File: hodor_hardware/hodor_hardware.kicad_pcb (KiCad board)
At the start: 2 copper layers, 259 parts, among them J1 Screw_Terminal_01x02, J10 Screw_Terminal_01x03, J2 Screw_Terminal_01x05, J3 Screw_Terminal_01x03, J4 USB_C_Receptacle_USB2.0_16P, J5 Screw_Terminal_01x03, J6 Screw_Terminal_01x04, J7 Screw_Terminal_01x02, J8 Conn_01x04_Pin, J9 Conn_01x04_Pin, K1 FINDER-32.21-x000, K2 FINDER-32.21-x000, Q1 SiS443DN, Q10 BC847BDW1, Q2 FDG1024NZ, Q3 FDG1024NZ, Q4 FDG1024NZ, Q5 BSS138, Q6 BSS138DW, Q7 SiS443DN, Q8 2V7002, Q9 DMP6050SSD, SW1 SW_RST, SW2 SW_BOOT, T1 GND, T10 V_{BUS}, T11 3V3, T12 5V, T14 V_{BUS}_SENSE, T15 I_SNS, T16 D_FB, T17 D_PWM2, T18 D_PWM1, T19 VC_OUT, T20 V_LDSNS, T21 SCL, T22 VC_CMP, T23 VC_REF, T24 SDA, T25 DRV_EN, T26 DRV_SF, T27 SF_Q, T28 SF_TRG, T29 SF_CLR, T30 ENC_B, T31 ENC_A, T32 GND, T4 IN2, T5 IN1, T6 V_{DC}_SENSE, T7 IN3, T8 IN4, T9 V_{DC}, U1 ESP32-S3-WROOM-1_N8R2, U10 LM4040DBZ-2.5, U11 MCP6561x-LT, U12 MC33HB2002, U13 74LVC1G123, U14 ACS722xLCTR-10AB, U2 TLV62569DBV, U3 74LVC2G14, U4 74LVC2G14, U5 TPS54240DRC, U6 MAX811SEUS-T, U7 74LVC2G14, U8 ZXTR2105F, U9 24LC256

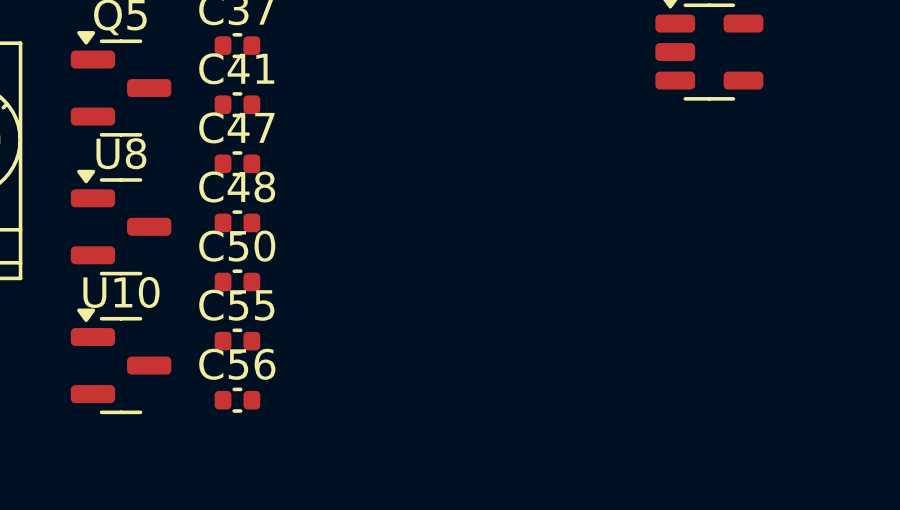
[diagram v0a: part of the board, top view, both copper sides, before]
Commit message: Added USB switchover function for 5V
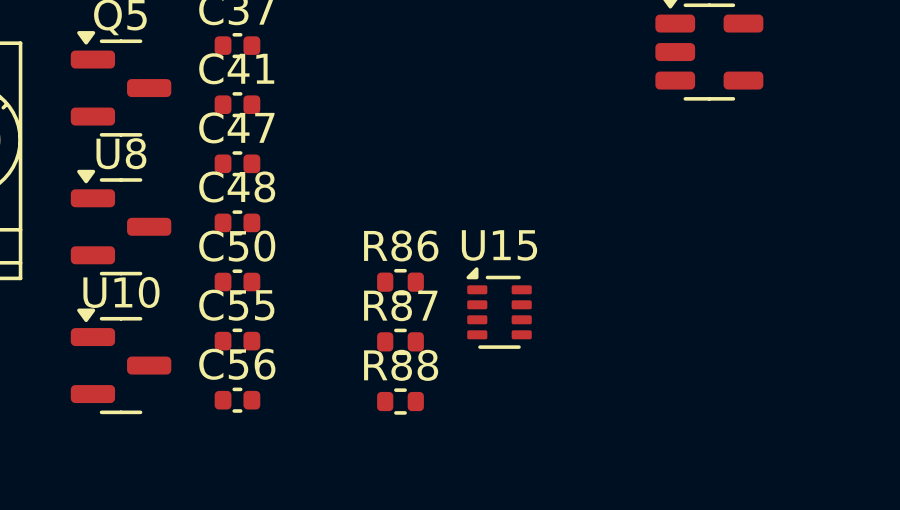
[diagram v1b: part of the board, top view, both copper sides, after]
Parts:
- added R86: 10k, Resistor_SMD:R_0402_1005Metric, F.Cu at (65.6, 114.0)
- added R87: 0R, Resistor_SMD:R_0402_1005Metric, F.Cu at (65.6, 116.0)
- added R88: 10k, Resistor_SMD:R_0402_1005Metric, F.Cu at (65.6, 118.0)
- added U15: TPS2116DRL, Package_TO_SOT_SMD:SOT-583-8, F.Cu at (68.9, 115.0)
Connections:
- C18 pad 1: Net-(D17-A) -> 5V_USB
- C19 pad 2: Net-(D17-A) -> 5V_USB
- C58 pad 1: +5V -> Net-(U15-MODE)
- C66 pad 1: +5V -> Net-(U15-MODE)
- C67 pad 1: +5V -> Net-(U15-MODE)
- C68 pad 1: +5V -> Net-(U15-MODE)
- C69 pad 1: +5V -> Net-(U15-MODE)
- C70 pad 1: +5V -> Net-(U15-MODE)
- L13 pad 2: +5V -> Net-(U15-MODE)
- L2 pad 1: Net-(D17-A) -> 5V_USB
- R73 pad 2: +5V -> Net-(U15-MODE)

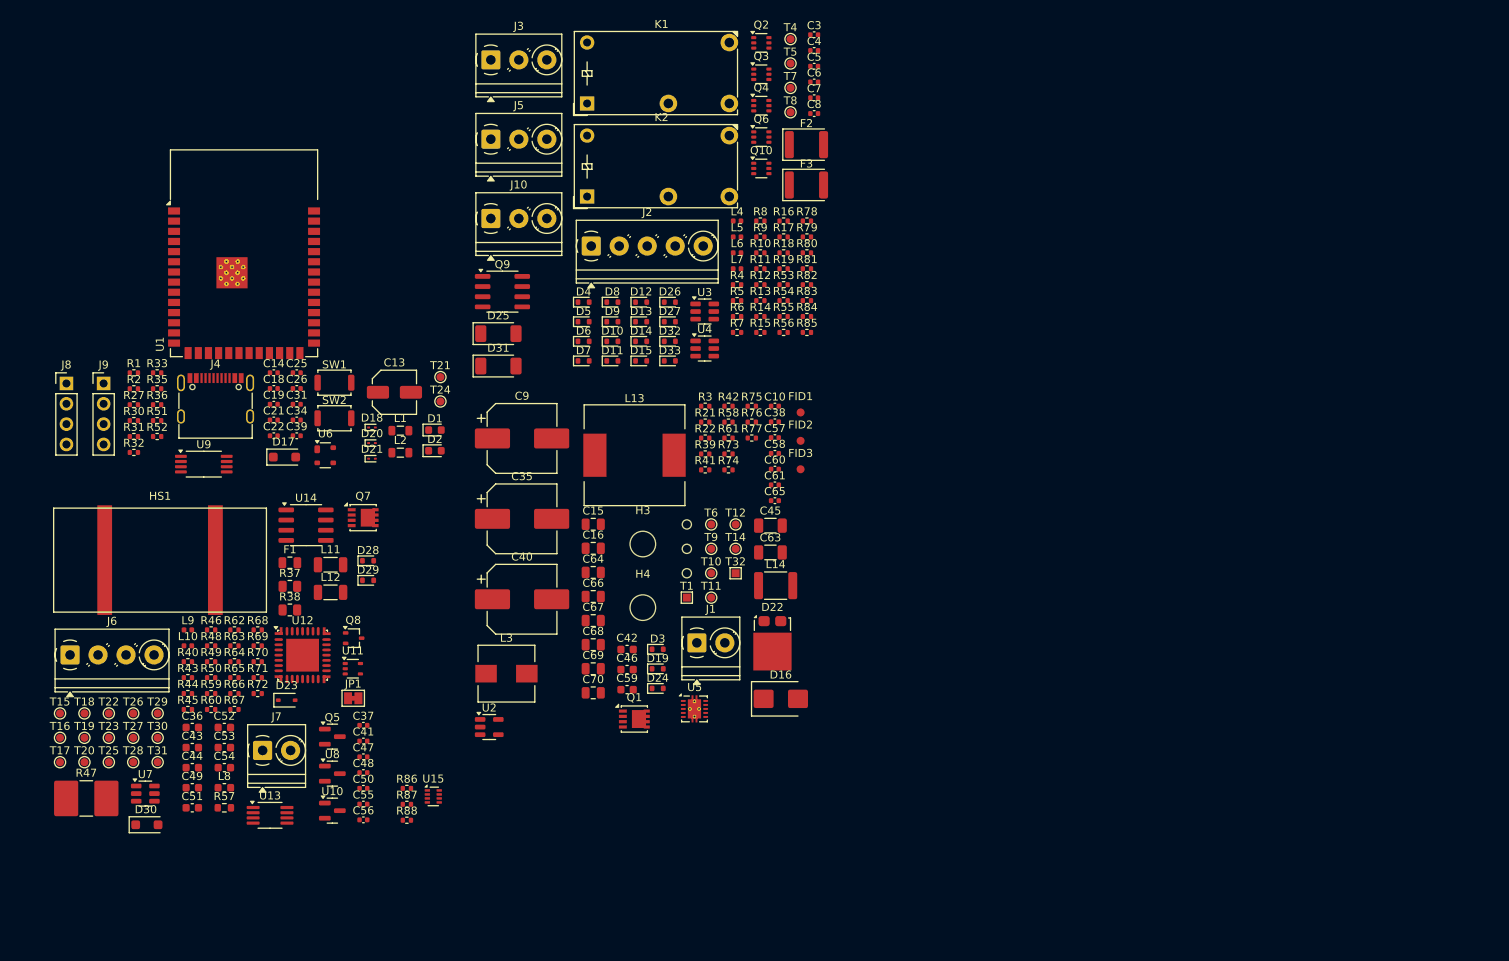
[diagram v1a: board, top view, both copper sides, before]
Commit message: Reworked into 2 PCBs
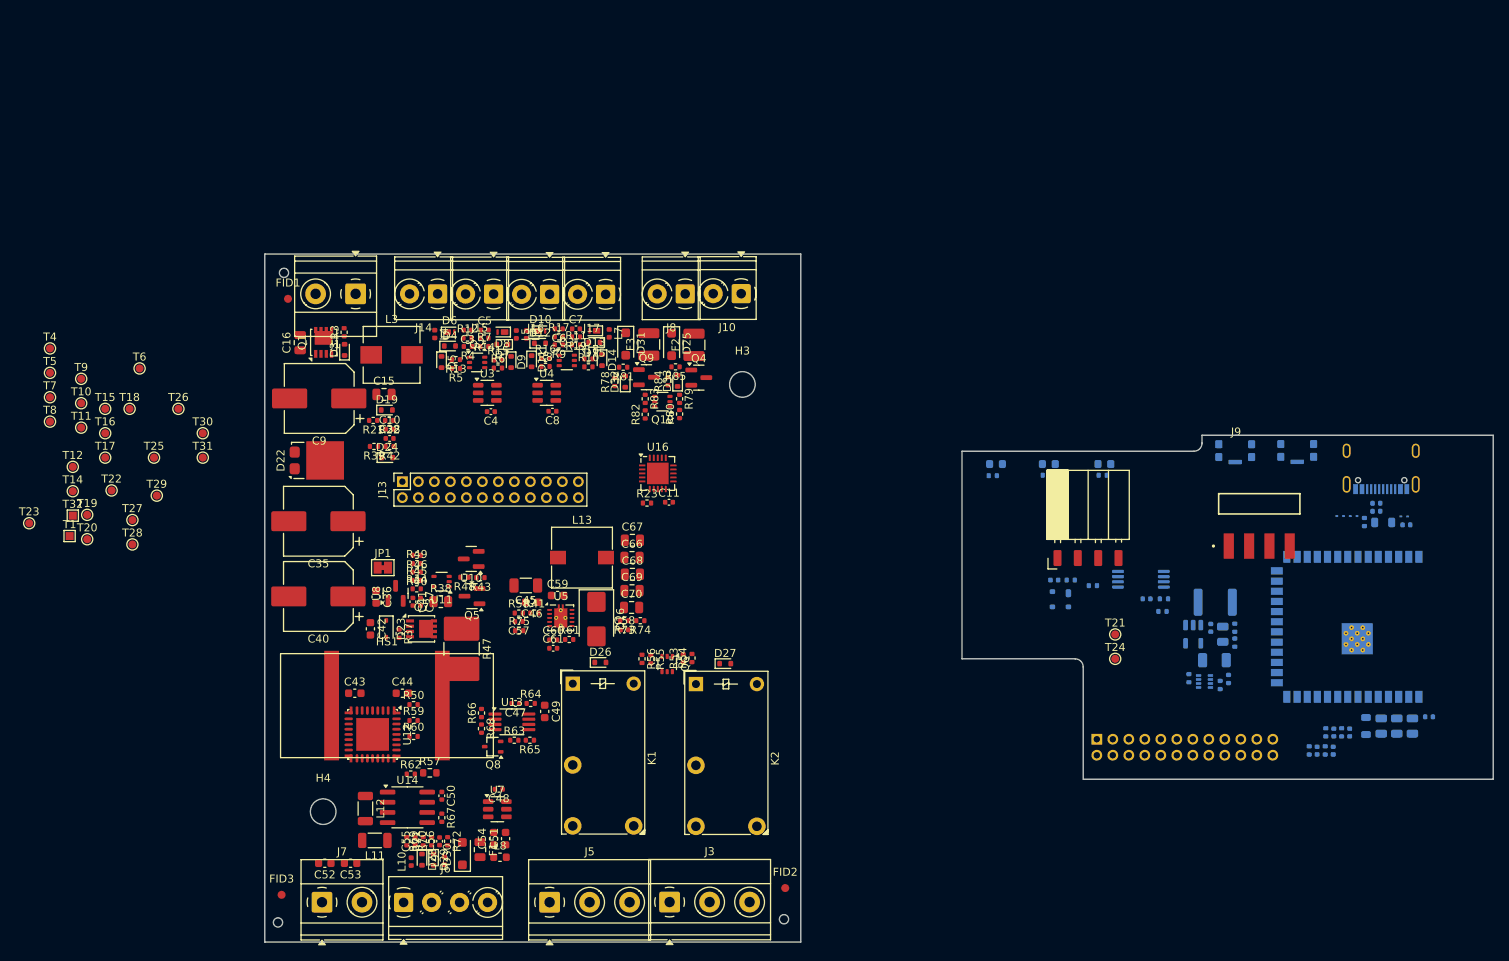
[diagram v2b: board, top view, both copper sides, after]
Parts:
- removed C13: 47u/10V, Capacitor_SMD:C_Elec_5x5.4
- removed J2: Screw_Terminal_01x05, TerminalBlock_Phoenix:TerminalBlock_Phoenix_PT-1,5-5-3.5-H_1x05_P3.50mm_Horizontal
- added C11: 100nF, Capacitor_SMD:C_0402_1005Metric, F.Cu at (98.3, 78.2)
- added C71: 10uF, Capacitor_SMD:C_0805_2012Metric, B.Cu at (187.3, 106.2)
- added C72: 10uF, Capacitor_SMD:C_0805_2012Metric, B.Cu at (189.3, 106.2)
- added C73: 10uF, Capacitor_SMD:C_0805_2012Metric, B.Cu at (191.2, 106.2)
- added J12: Conn_01x24_Pin, Connector_PinHeader_2.00mm:PinHeader_2x12_P2.00mm_Horizontal, B.Cu at (151.8, 107.8)
- added J13: Conn_01x24_Socket, Connector_PinSocket_2.00mm:PinSocket_2x12_P2.00mm_Vertical, F.Cu at (65.0, 75.7)
- added J14: Screw_Terminal_01x02, TerminalBlock_Phoenix:TerminalBlock_Phoenix_PT-1,5-2-3.5-H_1x02_P3.50mm_Horizontal, F.Cu at (69.4, 52.2)
- added J15: Screw_Terminal_01x02, TerminalBlock_Phoenix:TerminalBlock_Phoenix_PT-1,5-2-3.5-H_1x02_P3.50mm_Horizontal, F.Cu at (76.4, 52.2)
- added J16: Screw_Terminal_01x02, TerminalBlock_Phoenix:TerminalBlock_Phoenix_PT-1,5-2-3.5-H_1x02_P3.50mm_Horizontal, F.Cu at (83.4, 52.2)
- added J17: Screw_Terminal_01x02, TerminalBlock_Phoenix:TerminalBlock_Phoenix_PT-1,5-2-3.5-H_1x02_P3.50mm_Horizontal, F.Cu at (90.4, 52.2)
- added R20: 220R, Resistor_SMD:R_0402_1005Metric, B.Cu at (152.5, 74.8)
- added R23: 10k, Resistor_SMD:R_0402_1005Metric, F.Cu at (95.6, 78.3)
- added U16: MCP23S08-xML, Package_DFN_QFN:QFN-20-1EP_4x4mm_P0.5mm_EP2.7x2.7mm, F.Cu at (96.9, 74.6)
- added U17: SSD1306, hodor_footprints:SSD1306_OLED_Horizontal_Reverse, F.Cu at (150.7, 85.2)
- C14, C18, C19, C21, C22, C25, C26, C31, C34, C39, C63, C64, C65, D18, D20, D21, J4, L1, L14, L2, R1, R2, R27, R30, R31, R32, R33, R35, R36, R51, R52, R76, R77, R86, R87, R88, U1, U15, U2, U6, U9: moved to B.Cu
- D1, D2: footprint LED_SMD:LED_0603_1608Metric -> LED_SMD:LED_Kingbright_APA1606_1.6x0.6mm_Horizontal; moved to B.Cu
- D10, D13, D6, D8: footprint Diode_SMD:D_SOD-523 -> Diode_SMD:Nexperia_DSN1608-2_1.6x0.8mm
- D17: value PMEG6010 -> blue; footprint Diode_SMD:D_SOD-123F -> LED_SMD:LED_Kingbright_APA1606_1.6x0.6mm_Horizontal; moved to B.Cu
- D25, D31: footprint Diode_SMD:D_SOD-128 -> Diode_SMD:D_SOD-123F
- F2, F3: footprint Diode_SMD:D_1812_4532Metric -> Fuse:Fuse_1210_3225Metric
- J1, J7: footprint TerminalBlock_Phoenix:TerminalBlock_Phoenix_PT-1,5-2-3.5-H_1x02_P3.50mm_Horizontal -> TerminalBlock_Phoenix:TerminalBlock_Phoenix_MKDS-1,5-2_1x02_P5.00mm_Horizontal
- J10: value Screw_Terminal_01x03 -> Screw_Terminal_01x02; footprint TerminalBlock_Phoenix:TerminalBlock_Phoenix_PT-1,5-3-3.5-H_1x03_P3.50mm_Horizontal -> TerminalBlock_Phoenix:TerminalBlock_Phoenix_PT-1,5-2-3.5-H_1x02_P3.50mm_Horizontal
- J3, J5: footprint TerminalBlock_Phoenix:TerminalBlock_Phoenix_PT-1,5-3-3.5-H_1x03_P3.50mm_Horizontal -> TerminalBlock_Phoenix:TerminalBlock_Phoenix_MKDS-1,5-3_1x03_P5.00mm_Horizontal
- J8: value Conn_01x04_Pin -> Screw_Terminal_01x02; footprint Connector_PinHeader_2.54mm:PinHeader_1x04_P2.54mm_Vertical -> TerminalBlock_Phoenix:TerminalBlock_Phoenix_PT-1,5-2-3.5-H_1x02_P3.50mm_Horizontal
- J9: footprint Connector_PinHeader_2.54mm:PinHeader_1x04_P2.54mm_Vertical -> hodor_footprints:Conn_Header2.54_1x04_SMD
- L13: footprint Inductor_SMD:L_12x12mm_H6mm -> Inductor_SMD:L_Wuerth_WE-PD-Typ-7345
- Q4: value FDG1024NZ -> IRLML9301; footprint Package_TO_SOT_SMD:SOT-363_SC-70-6 -> Package_TO_SOT_SMD:SOT-23
- Q9: value DMP6050SSD -> IRLML9301; footprint Package_SO:SOIC-8_3.9x4.9mm_P1.27mm -> Package_TO_SOT_SMD:SOT-23
- R37: value 1k -> 10k; footprint Resistor_SMD:R_0805_2012Metric -> Resistor_SMD:R_0402_1005Metric
- R38: value 1.5k -> 2k
- SW1, SW2: footprint Button_Switch_SMD:SW_Push_SPST_NO_Alps_SKRK -> Button_Switch_SMD:SW_SPST_CK_KMS2xxG; moved to B.Cu
- moved R31 155.4 mm to (182.4, 107.0), turned to 90 degrees
- moved R30 154.0 mm to (180.4, 107.0), turned to 90 degrees
- moved R32 153.5 mm to (180.3, 109.2), turned to 90 degrees
- moved R35 151.8 mm to (185.2, 80.7), turned to 90 degrees
- moved R36 150.4 mm to (178.3, 109.2), turned to 90 degrees
- moved U1 149.1 mm to (186.8, 93.8), turned to 90 degrees
- moved C26 147.4 mm to (193.3, 105.0), turned to 180 degrees
- moved J4 145.8 mm to (187.3, 72.9)
- moved J9 145.2 mm to (172.1, 78.4)
- moved C31 139.5 mm to (190.5, 81.0), turned to 180 degrees
- moved C22 139.5 mm to (183.4, 107.0), turned to 90 degrees
- moved C18 138.6 mm to (186.8, 78.3)
- moved C19 138.5 mm to (186.8, 79.3), turned to 180 degrees
- moved C21 138.1 mm to (181.4, 107.0), turned to 90 degrees
- moved C25 137.9 mm to (181.3, 109.3), turned to 90 degrees
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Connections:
- net /Controller/ADC_IN1 renamed /Controllerboard/ADC_IN1
- net /Controller/ADC_IN2 renamed /Controllerboard/ADC_IN2
- net /Controller/ADC_IN3 renamed /Controllerboard/ADC_IN3
- net /Controller/ADC_IN4 renamed /Controllerboard/ADC_IN4
- net /Controller/USB_D+ renamed /Controllerboard/USB_D+
- net /Controller/USB_D- renamed /Controllerboard/USB_D-
- C10 pad 1: /Controller/ADC_CH2 -> /Controllerboard/ADC_CH2
- C14 pad 1: GND -> GNDD
- C14 pad 2: +3V3 -> VD3V3
- C18 pad 2: GND -> GNDD
- C19 pad 1: GND -> GNDD
- C21 pad 1: GND -> GNDD
- C22 pad 1: GND -> GNDD
- C25 pad 1: GND -> GNDD
- C26 pad 1: GND -> GNDD
- C31 pad 2: GND -> GNDD
- C34 pad 1: GND -> GNDD
- C38 pad 1: /Controller/ADC_CH1 -> /Controllerboard/ADC_CH1
- C39 pad 1: GND -> GNDD
- C39 pad 2: +3V3 -> VD3V3
- C52 pad 2: Net-(J7-Pin_2) -> Net-(J7-Pin_1)
- C53 pad 1: Net-(J7-Pin_1) -> Net-(J7-Pin_2)
- C58 pad 1: Net-(U15-MODE) -> +5V
- C63 pad 1: +5V -> Net-(U2-EN)
- C63 pad 2: GND -> GNDD
- C64 pad 1: +3V3 -> VD3V3
- C64 pad 2: GND -> GNDD
- C65 pad 1: +3V3 -> VD3V3
- C65 pad 2: GND -> GNDD
- C66 pad 1: Net-(U15-MODE) -> +5V
- C67 pad 1: Net-(U15-MODE) -> +5V
- C68 pad 1: Net-(U15-MODE) -> +5V
- C69 pad 1: Net-(U15-MODE) -> +5V
- C70 pad 1: Net-(U15-MODE) -> +5V
- D1 pad 1: GND -> GNDD
- D17 pad 1: +5V -> GNDD
- D18 pad 1: GND -> GNDD
- D19 pad 1: /Controller/ADC_CH2 -> /Controllerboard/ADC_CH2
- D2 pad 1: GND -> GNDD
- D20 pad 1: GND -> GNDD
- D21 pad 1: GND -> GNDD
- D24 pad 1: /Controller/ADC_CH1 -> /Controllerboard/ADC_CH1
- F2 pad 1: Net-(F2-Pad1) -> Net-(Q4-D)
- F3 pad 1: Net-(F3-Pad1) -> Net-(Q9-D)
- J10 pad 1: GND -> Net-(D25-K)
- J10 pad 2: Net-(D31-K) -> GND
- J4 pad A1: GND -> GNDD
- J4 pad A12: GND -> GNDD
- J4 pad B1: GND -> GNDD
- J4 pad B12: GND -> GNDD
- J8 pad 1: GND -> Net-(D31-K)
- J8 pad 2: /Controller/SCL -> GND
- J9 pad 1: GND -> GNDD
- J9 pad 2: /Controller/RXD -> /Controllerboard/TXD
- J9 pad 3: /Controller/TXD -> /Controllerboard/RXD
- J9 pad 4: +3V3 -> VD3V3
- K1 pad 12: Net-(J5-Pin_1) -> Net-(J5-Pin_3)
- K1 pad 14: Net-(J5-Pin_3) -> Net-(J5-Pin_1)
- K2 pad 12: Net-(J3-Pin_1) -> Net-(J3-Pin_3)
- K2 pad 14: Net-(J3-Pin_3) -> Net-(J3-Pin_1)
- L1 pad 1: +3V3 -> VD3V3
- L11 pad 2: Net-(J7-Pin_1) -> Net-(J7-Pin_2)
- L12 pad 2: Net-(J7-Pin_2) -> Net-(J7-Pin_1)
- L13 pad 2: Net-(U15-MODE) -> +5V
- L14 pad 2: +3V3 -> VD3V3
- Q4 pad 1: (no net) -> Net-(D32-A)
- Q4 pad 2: (no net) -> V_{DC}
- Q4 pad 3: Net-(D15-A) -> Net-(Q4-D)
- Q9 pad 1: V_{DC} -> Net-(D33-A)
- Q9 pad 2: Net-(D32-A) -> V_{DC}
- Q9 pad 3: V_{DC} -> Net-(Q9-D)
- R1 pad 1: Net-(U1-IO14) -> /Controllerboard/LED_ACTIVE
- R2 pad 1: Net-(U1-IO9) -> /Controllerboard/LED_STATUS
- R21 pad 1: /Controller/ADC_CH2 -> /Controllerboard/ADC_CH2
- R22 pad 2: /Controller/ADC_CH2 -> /Controllerboard/ADC_CH2
- R27 pad 2: GND -> GNDD
- R30 pad 1: /Controller/ADC_CH2 -> Net-(J12-Pin_2)
- R31 pad 1: /Controller/ADC_CH1 -> Net-(J12-Pin_1)
- R32 pad 1: /Controller/ADC_CH3 -> Net-(J12-Pin_3)
- R33 pad 2: GND -> GNDD
- R35 pad 2: GND -> GNDD
- R36 pad 1: /Controller/ADC_CH4 -> Net-(J12-Pin_4)
- R39 pad 1: /Controller/ADC_CH1 -> /Controllerboard/ADC_CH1
- R42 pad 2: /Controller/ADC_CH1 -> /Controllerboard/ADC_CH1
- R50 pad 1: /Controller/DRV_EN -> /Controllerboard/DRV_EN
- R51 pad 1: +3V3 -> Net-(U1-3V3)
- R51 pad 2: /Controller/SCL -> /Controllerboard/SCL
- R52 pad 1: +3V3 -> Net-(U1-3V3)
- R52 pad 2: /Controller/SDA -> /Controllerboard/SDA
- R54 pad 2: /Controller/RELAY_CTRL_1 -> /Peripherals/REL_CTRL_1
- R56 pad 2: /Controller/RELAY_CTRL_2 -> /Peripherals/REL_CTRL_2
- R57 pad 1: /Controller/ADC_CH3 -> /Controllerboard/ADC_CH3
- R59 pad 2: /Controller/~{CS} -> /Controllerboard/~{CS0}
- R62 pad 2: /Controller/DRV_~{SF} -> /Controllerboard/DRV_~{SF}
- R66 pad 1: /Controller/SAFETY_TRIG -> /Controllerboard/SAFETY_TRIG
- R68 pad 1: /Controller/SAFETY_~{CLR} -> /Controllerboard/SAFETY_~{CLR}
- R73 pad 2: Net-(U15-MODE) -> +5V
- R76 pad 2: +3V3 -> VD3V3
- R77 pad 1: GND -> GNDD
- R79 pad 1: /Controller/OUT_CTRL_1 -> /Peripherals/OUT_CTRL_1
- R82 pad 1: /Controller/OUT_CTRL_2 -> /Peripherals/OUT_CTRL_2
- R86 pad 2: +5V -> Net-(U2-EN)
- R87 pad 2: Net-(U15-MODE) -> 5V_BOARD
- R88 pad 1: GND -> GNDD
- SW1 pad 1: GND -> GNDD
- SW2 pad 1: GND -> GNDD
- T14 pad 1: /Controller/ADC_CH1 -> /Controllerboard/ADC_CH1
- T15 pad 1: /Controller/ADC_CH4 -> /Controllerboard/ADC_CH4
- T16 pad 1: /Controller/ADC_CH3 -> /Controllerboard/ADC_CH3
- T17 pad 1: /Controller/DRV_PWM2 -> /Controllerboard/DRV_PWM2
- T18 pad 1: /Controller/DRV_PWM1 -> /Controllerboard/DRV_PWM1
- T21 pad 1: /Controller/SCL -> /Controllerboard/SCL
- T24 pad 1: /Controller/SDA -> /Controllerboard/SDA
- T25 pad 1: /Controller/DRV_EN -> /Controllerboard/DRV_EN
- T26 pad 1: /Controller/DRV_~{SF} -> /Controllerboard/DRV_~{SF}
- T28 pad 1: /Controller/SAFETY_TRIG -> /Controllerboard/SAFETY_TRIG
- T29 pad 1: /Controller/SAFETY_~{CLR} -> /Controllerboard/SAFETY_~{CLR}
- T30 pad 1: /Controller/ENCODER_B -> /Controllerboard/ENCODER_B
- T31 pad 1: /Controller/ENCODER_A -> /Controllerboard/ENCODER_A
- T4 pad 1: /Controller/INPUT_2 -> /Peripherals/INPUT_2
- T5 pad 1: /Controller/INPUT_1 -> /Peripherals/INPUT_1
- T6 pad 1: /Controller/ADC_CH2 -> /Controllerboard/ADC_CH2
- T7 pad 1: /Controller/INPUT_3 -> /Peripherals/INPUT_3
- T8 pad 1: /Controller/INPUT_4 -> /Peripherals/INPUT_4
- U1 pad 1: GND -> GNDD
- U1 pad 10: /Controller/OUT_CTRL_1 -> unconnected-(U1-IO17-Pad10)
- U1 pad 11: /Controller/OUT_CTRL_2 -> unconnected-(U1-IO18-Pad11)
- U1 pad 16: /Controller/DRV_~{SF} -> /Controllerboard/D_~{SF}
- U1 pad 17: Net-(U1-IO9) -> /Controllerboard/SPI_~{CS1}
- U1 pad 18: /Controller/~{CS} -> /Controllerboard/SPI_~{CS0}
- U1 pad 19: /Controller/MISO -> /Controllerboard/SPI_MISO
- U1 pad 20: /Controller/SCK -> /Controllerboard/SPI_SCK
- U1 pad 21: /Controller/MOSI -> /Controllerboard/SPI_MOSI
- U1 pad 22: Net-(U1-IO14) -> unconnected-(U1-IO14-Pad22)
- U1 pad 24: /Controller/DRV_PWM1 -> /Controllerboard/D_PWM1
- U1 pad 25: /Controller/DRV_PWM2 -> /Controllerboard/D_PWM2
- U1 pad 26: /Controller/DRV_EN -> /Controllerboard/D_EN
- U1 pad 28: /Controller/ENCODER_A -> /Controllerboard/ENC_A
- U1 pad 29: /Controller/ENCODER_B -> /Controllerboard/ENC_B
- U1 pad 30: /Controller/INPUT_1 -> unconnected-(U1-IO37-Pad30)
- U1 pad 31: /Controller/INPUT_2 -> unconnected-(U1-IO38-Pad31)
- U1 pad 32: /Controller/INPUT_3 -> unconnected-(U1-IO39-Pad32)
- U1 pad 33: /Controller/INPUT_4 -> unconnected-(U1-IO40-Pad33)
- U1 pad 34: /Controller/SAFETY_~{CLR} -> /Controllerboard/SF_~{CLR}
- U1 pad 35: /Controller/SAFETY_TRIG -> /Controllerboard/SF_TRG
- U1 pad 36: /Controller/RXD -> /Controllerboard/RXD
- U1 pad 37: /Controller/TXD -> /Controllerboard/TXD
- U1 pad 38: /Controller/SDA -> /Controllerboard/SDA
- U1 pad 39: /Controller/SCL -> /Controllerboard/SCL
- U1 pad 40: GND -> GNDD
- U1 pad 41: GND -> GNDD
- U1 pad 8: /Controller/RELAY_CTRL_1 -> unconnected-(U1-IO15-Pad8)
- U1 pad 9: /Controller/RELAY_CTRL_2 -> unconnected-(U1-IO16-Pad9)
- U12 pad 1: /Controller/MISO -> /Controllerboard/MISO
- U12 pad 10: /Controller/ADC_CH3 -> /Controllerboard/ADC_CH3
- U12 pad 15: /Controller/DRV_~{SF} -> /Controllerboard/DRV_~{SF}
- U12 pad 2: /Controller/SCK -> /Controllerboard/SCK
- U12 pad 27: /Controller/~{CS} -> /Controllerboard/~{CS0}
- U12 pad 3: /Controller/MOSI -> /Controllerboard/MOSI
- U12 pad 6: /Controller/DRV_EN -> /Controllerboard/DRV_EN
- U12 pad 8: /Controller/DRV_PWM2 -> /Controllerboard/DRV_PWM2
- U12 pad 9: /Controller/DRV_PWM1 -> /Controllerboard/DRV_PWM1
- U13 pad 2: /Controller/SAFETY_TRIG -> /Controllerboard/SAFETY_TRIG
- U13 pad 3: /Controller/SAFETY_~{CLR} -> /Controllerboard/SAFETY_~{CLR}
- U14 pad 7: /Controller/ADC_CH4 -> /Controllerboard/ADC_CH4
- U15 pad 1: GND -> GNDD
- U15 pad 2: +5V -> Net-(U2-EN)
- U15 pad 3: Net-(U15-MODE) -> 5V_BOARD
- U15 pad 5: Net-(U15-MODE) -> 5V_BOARD
- U15 pad 7: +5V -> Net-(U2-EN)
- U2 pad 1: +5V -> Net-(U2-EN)
- U2 pad 2: GND -> GNDD
- U2 pad 4: +5V -> Net-(U2-EN)
- U3 pad 4: /Controller/INPUT_2 -> /Peripherals/INPUT_2
- U3 pad 6: /Controller/INPUT_1 -> /Peripherals/INPUT_1
- U4 pad 4: /Controller/INPUT_4 -> /Peripherals/INPUT_4
- U4 pad 6: /Controller/INPUT_3 -> /Peripherals/INPUT_3
- U6 pad 1: GND -> GNDD
- U6 pad 4: +3V3 -> VD3V3
- U7 pad 4: /Controller/ENCODER_B -> /Controllerboard/ENCODER_B
- U7 pad 6: /Controller/ENCODER_A -> /Controllerboard/ENCODER_A
- U9 pad 1: GND -> GNDD
- U9 pad 2: GND -> GNDD
- U9 pad 3: GND -> GNDD
- U9 pad 4: GND -> GNDD
- U9 pad 5: /Controller/SDA -> /Controllerboard/SDA
- U9 pad 6: /Controller/SCL -> /Controllerboard/SCL
- U9 pad 7: GND -> GNDD
- U9 pad 8: +3V3 -> VD3V3
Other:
- board outline added: 153.6 x 86 mm
- board text added: "-"
- board text added: "01.02.2017"
- board text added: "044934011"
- board text added: "044934055"
- board text added: "1"
- board text added: "1/1"
- board text added: "1:1"
- board text added: "2"
- board text added: "3"
- board text added: "4"
- board text added: "449-340-11"
- board text added: "449-340-56"
- board text added: "5"
- board text added: "6"
- board text added: "7"
- board text added: "8"
- board text added: "A"
- board text added: "B"
- board text added: "BENENNUNG"
- board text added: "BESCHREIBUNG"
- board text added: "Bearb."
- board text added: "Benennung"
- board text added: "Blatt"
- board text added: "D.Haas"
- board text added: "Datum"
- board text added: "Gepr."
- board text added: "Gewerbegebiet D-54552 Mehren"
- board text added: "Housing: Apra-Rail DB4"
- board text added: "J.Schmitz"
- board text added: "Klemmen"
- board text added: "MENGE"
- board text added: "Material:"
- board text added: "Name"
- board text added: "POS-NR."
- board text added: "Progr."
- board text added: "SCHNITT A-A"
- board text added: "SCHNITT B-B"
- board text added: "Unterschale 4DB"
- board text added: "Unterschale DB 3"
- board text added: "Version"
- board text added: "Zeichnungsnummer"
- board text added: "apra-norm Elektromechanik GmbH"
- board text added: "apraRail DB4"
- board text added: "neu erstellt"
